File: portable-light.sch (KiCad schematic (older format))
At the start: 11 parts, among them J3 Charger, U1 L78L05_SOT89

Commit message: Schematic's overall structure is finished
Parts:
- added D?: 1N5819, Diode_THT:D_DO-41_SOD81_P12.70mm_Horizontal, symbol portable-light-rescue:1N5819-Diode
- added J?: LOAD, Connector_PinHeader_2.54mm:PinHeader_1x02_P2.54mm_Vertical, symbol portable-light-rescue:LED-Device
- renumbered BT1 to BT?, C27 to C?, C21 to C?, C17 to C?, D9 to D?, D8 to D?, J3 to J?, NT1 to NT?, NT2 to NT?, R26 to R?, U1 to U?
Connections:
- net +8V: now also D?.1 (K)
- net GNDPWR: now also J?.1 (K)
- net at C?.1, D?.2 (A), U?.1 (OUT): now also D?.2 (A)
- new net Buck converter/vout: J?.2 (A)
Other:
- moved on the sheet: BT?, C?, D?, J?, NT?, R?, U?

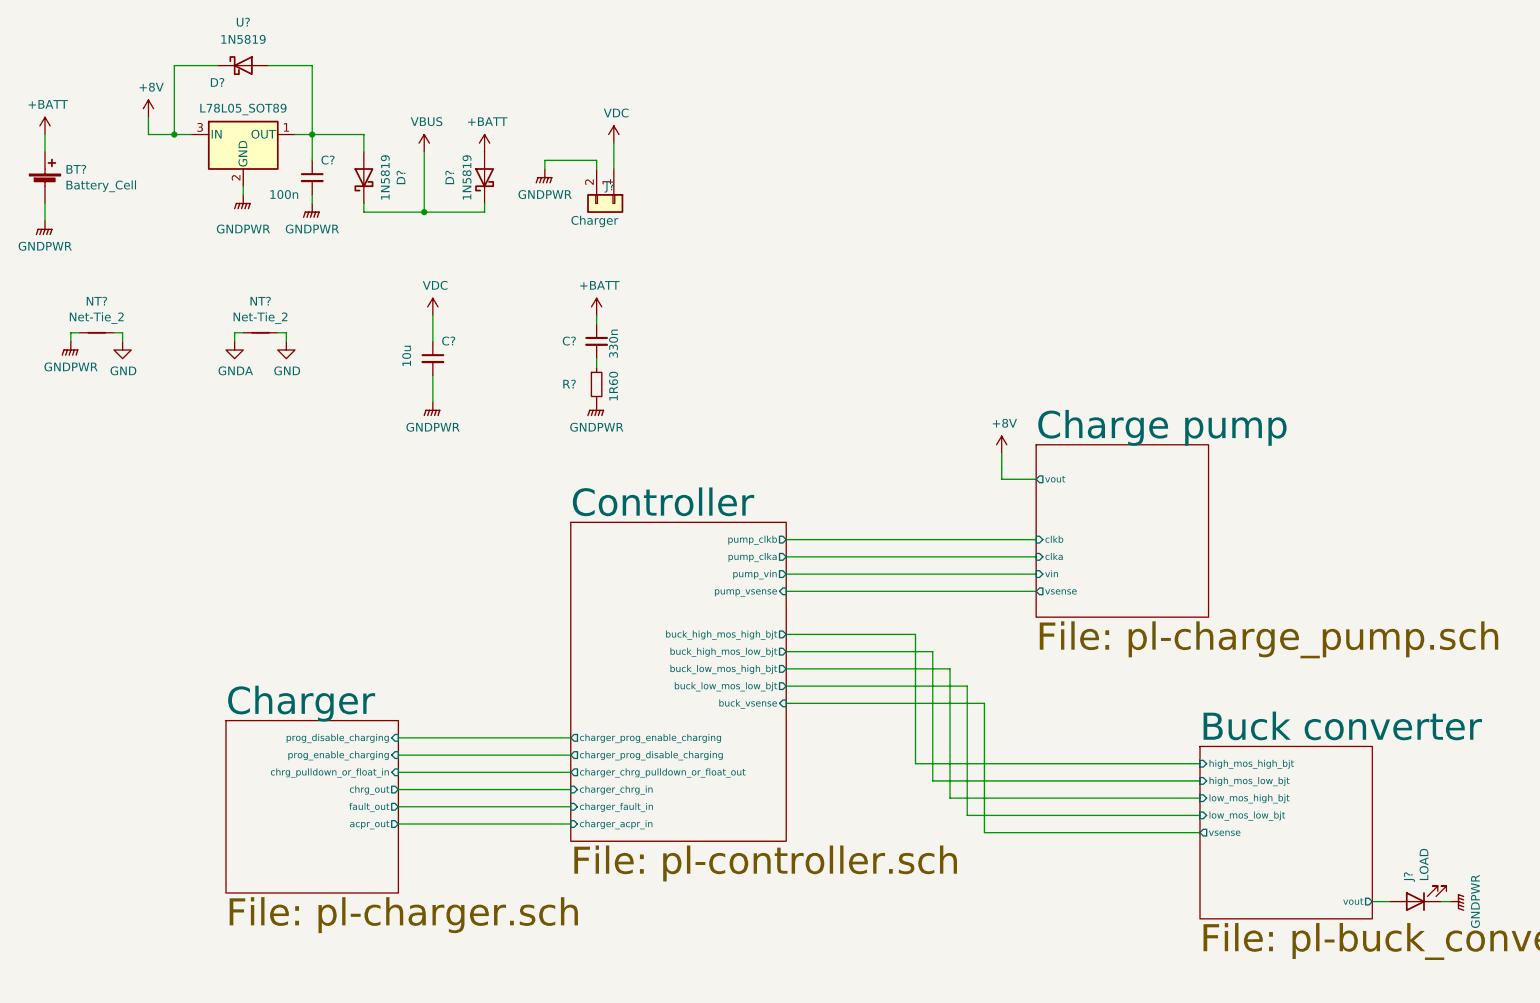
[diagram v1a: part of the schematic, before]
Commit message: Added component values
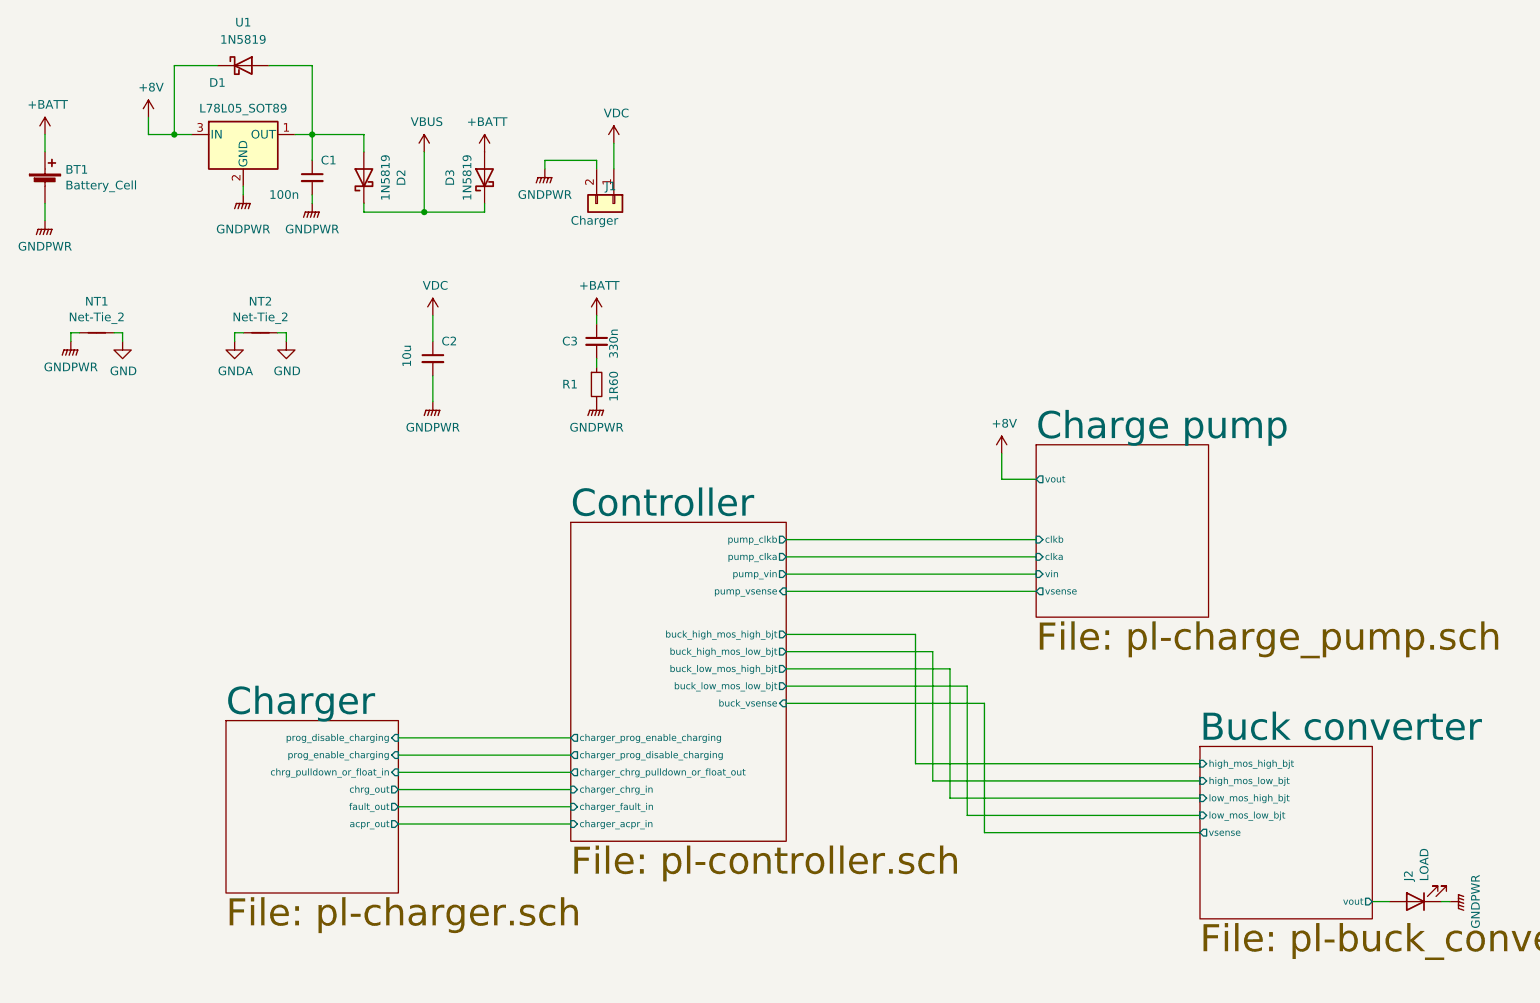
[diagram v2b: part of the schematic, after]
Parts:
- gave numbers to parts that had none: 13

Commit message: Schematics redesigned and fixed
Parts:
- removed C2: 10u, Capacitor_THT:C_Radial_D5.0mm_H7.0mm_P2.00mm, symbol portable-light-rescue:C_Small-Device
- removed C3: 330n, Capacitor_SMD:C_1206_3216Metric_Pad1.42x1.75mm_HandSolder, symbol portable-light-rescue:C_Small-Device
- removed D1, D2, D3: 1N5819, Diode_THT:D_DO-41_SOD81_P12.70mm_Horizontal, symbol portable-light-rescue:1N5819-Diode
- removed J1: Charger, Connector_PinHeader_2.54mm:PinHeader_1x02_P2.54mm_Vertical, symbol portable-light-rescue:Conn_01x02-Connector_Generic
- removed NT1, NT2: Net-Tie_2, NetTie:NetTie-2_SMD_Pad0.5mm, symbol portable-light-rescue:Net-Tie_2-Device
- removed U1: L78L05_SOT89, Package_TO_SOT_SMD:SOT-89-3, symbol portable-light-rescue:L78L05_SOT89-Regulator_Linear
- added J2: conn_sense_pump_2, Ribbon_Cable:Ribbon_2, symbol Connector_Generic:Conn_01x02
- added J3: conn_sense_buck_2, Ribbon_Cable:Ribbon_2, symbol Connector_Generic:Conn_01x02
- added J4: conn_batt_2, Connector_PinHeader_2.54mm:PinHeader_1x02_P2.54mm_Vertical, symbol Connector_Generic:Conn_01x02
- added J5: conn_batt_1, Connector_PinHeader_2.54mm:PinHeader_1x02_P2.54mm_Vertical, symbol Connector_Generic:Conn_01x02
- added J6: conn_sense_pump_1, Ribbon_Cable:Ribbon_2, symbol Connector_Generic:Conn_01x02
- added J7: conn_sense_buck_1, Ribbon_Cable:Ribbon_2, symbol Connector_Generic:Conn_01x02
- added J8: interboard-interface_2, Ribbon_Cable:Ribbon_8, symbol Connector_Generic:Conn_01x08
- added J9: interboard-interface_1, Ribbon_Cable:Ribbon_8, symbol Connector_Generic:Conn_01x08
- added NT1: Net-Tie_4_Cross, NetTie:NetTie-4_SMD_Pad0.5mm, symbol Device:Net-Tie_4_Cross
- C1: value 100n -> 330n
- renumbered J2 to J1
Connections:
- net labels added: +BATT-1, +BATT-2, +PUMP-1, +PUMP-2, GND-CHARGER, GNDPWR-2, buck_high_mos_high_bjt_1, buck_high_mos_high_bjt_2, buck_high_mos_low_bjt_1, buck_high_mos_low_bjt_2, buck_low_mos_high_bjt_1, buck_low_mos_high_bjt_2, buck_low_mos_low_bjt_1, buck_low_mos_low_bjt_2, gnd_vsense_buck_1, gnd_vsense_pump_1, pump_clka_1, pump_clka_2, pump_clkb_1, pump_clkb_2, pump_onoff_1, pump_onoff_2, vsense_buck_1, vsense_buck_2, vsense_pump_1, vsense_pump_2
- net labels removed: +8V, +BATT, VBUS, VDC
- wire segments 65 -> 41
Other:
- moved on the sheet: J1

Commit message: Cleaned up the PCB a little bit, Fixed some errors in schematics
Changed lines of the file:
@@
 Text Label 10100 2200 0    39   ~ 0
 buck_high_mos_high_bjt_2
+Text Label 10100 1900 0    39   ~ 0
+pump_clka_2
 Text Label 10100 1800 0    39   ~ 0
-pump_clka_2
-Text Label 10100 1900 0    39   ~ 0
 pump_clkb_2
 Text Label 10100 2000 0    39   ~ 0
 pump_onoff_2
+Text Label 10100 2400 0    39   ~ 0
+buck_low_mos_low_bjt_2
 Text Label 10100 2500 0    39   ~ 0
-buck_low_mos_low_bjt_2
-Text Label 10100 2400 0    39   ~ 0
 buck_low_mos_high_bjt_2
 Text Label 10100 2300 0    39   ~ 0

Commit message: Seperated the two PCBs successfully, All DRC errors fixed, gotta double check the circuit
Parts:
- removed NT1: Net-Tie_4_Cross, NetTie:NetTie-4_SMD_Pad0.5mm, symbol Device:Net-Tie_4_Cross
- added NT1: Net-Tie_3_Tee, NetTie:NetTie-3_SMD_Pad0.5mm, symbol Device:Net-Tie_3_Tee
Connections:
- net labels removed: GNDPWR-2
- wire segments 41 -> 39
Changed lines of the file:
@@
 P 4300 6700
 AR Path="/5F37658B/60438762" Ref="#PWR?"  Part="1"
-AR Path="/60438762" Ref="#PWR05"  Part="1"
-F 0 "#PWR05" H 4300 6500 50  0001 C CNN
+AR Path="/60438762" Ref="#PWR03"  Part="1"
+F 0 "#PWR03" H 4300 6500 50  0001 C CNN
 F 1 "GNDPWR" H 4300 6550 50  0000 C CNN
 F 2 "" H 4300 6650 50  0001 C CNN
@@
 gnd_vsense_buck_1
 $Comp
-L power:GNDA #PWR06
+L power:GNDA #PWR04
 U 1 1 5F835CEE
 P 8250 1800
-F 0 "#PWR06" H 8250 1550 50  0001 C CNN
+F 0 "#PWR04" H 8250 1550 50  0001 C CNN
 F 1 "GNDA" H 8255 1627 50  0000 C CNN
 F 2 "" H 8250 1800 50  0001 C CNN
@@
 $EndComp
 $Comp
-L power:GNDA #PWR07
+L power:GNDA #PWR05
 U 1 1 5F836352
 P 8250 2550
-F 0 "#PWR07" H 8250 2300 50  0001 C CNN
+F 0 "#PWR05" H 8250 2300 50  0001 C CNN
 F 1 "GNDA" H 8255 2377 50  0000 C CNN
 F 2 "" H 8250 2550 50  0001 C CNN
@@
 Text GLabel 10100 5650 2    39   UnSpc ~ 0
 +PUMP-1
-Wire Wire Line
-	2500 4000 2500 3950
 $Comp
 L portable-light-rescue:Battery_Cell-Device BT1
@@
 Text GLabel 2500 3500 1    39   UnSpc ~ 0
 +BATT-2
-$Comp
-L power:PWR_FLAG #FLG?
-U 1 1 5F8D18F2
-P 2500 3950
-AR Path="/5F378869/5F8D18F2" Ref="#FLG?"  Part="1"
-AR Path="/5F8D18F2" Ref="#FLG02"  Part="1"
-F 0 "#FLG02" H 2500 4025 50  0001 C CNN
-F 1 "PWR_FLAG" V 2500 4077 50  0000 L CNN
-F 2 "" H 2500 3950 50  0001 C CNN
-F 3 "~" H 2500 3950 50  0001 C CNN
-	1    2500 3950
-	0    -1   -1   0
-$EndComp
-Connection ~ 2500 3950
-Wire Wire Line
-	2500 3950 2500 3900
-$Comp
-L power:GND #PWR01
-U 1 1 5F8D1DCF
-P 2500 4000
-F 0 "#PWR01" H 2500 3750 50  0001 C CNN
-F 1 "GND" H 2505 3827 50  0000 C CNN
-F 2 "" H 2500 4000 50  0001 C CNN
-F 3 "" H 2500 4000 50  0001 C CNN
-	1    2500 4000
-	1    0    0    -1
-$EndComp
 Wire Wire Line
 	2500 3550 2500 3600
@@
 P 10700 2000
 AR Path="/5F378869/5F8E5DC5" Ref="#FLG?"  Part="1"
-AR Path="/5F8E5DC5" Ref="#FLG05"  Part="1"
-F 0 "#FLG05" H 10700 2075 50  0001 C CNN
+AR Path="/5F8E5DC5" Ref="#FLG06"  Part="1"
+F 0 "#FLG06" H 10700 2075 50  0001 C CNN
 F 1 "PWR_FLAG" V 10700 2300 50  0000 C CNN
 F 2 "" H 10700 2000 50  0001 C CNN
@@
 	10600 2100 10700 2100
 $Comp
-L power:GND #PWR04
-U 1 1 5F90484F
-P 3450 4000
-F 0 "#PWR04" H 3450 3750 50  0001 C CNN
-F 1 "GND" H 3455 3827 50  0000 C CNN
-F 2 "" H 3450 4000 50  0001 C CNN
-F 3 "" H 3450 4000 50  0001 C CNN
-	1    3450 4000
-	1    0    0    -1
-$EndComp
-Text GLabel 2700 4750 0    39   UnSpc ~ 0
-GNDPWR-2
-$Comp
 L power:GNDA #PWR02
 U 1 1 5F922DAB
-P 2950 4450
-F 0 "#PWR02" H 2950 4200 50  0001 C CNN
-F 1 "GNDA" H 2955 4277 50  0000 C CNN
-F 2 "" H 2950 4450 50  0001 C CNN
-F 3 "" H 2950 4450 50  0001 C CNN
-	1    2950 4450
-	-1   0    0    1
-$EndComp
-$Comp
-L power:GND #PWR03
+P 3350 4750
+F 0 "#PWR02" H 3350 4500 50  0001 C CNN
+F 1 "GNDA" H 3355 4577 50  0000 C CNN
+F 2 "" H 3350 4750 50  0001 C CNN
+F 3 "" H 3350 4750 50  0001 C CNN
+	1    3350 4750
+	0    -1   -1   0
+$EndComp
+$Comp
+L power:GND #PWR01
 U 1 1 5F924424
 P 2950 5000
-F 0 "#PWR03" H 2950 4750 50  0001 C CNN
+F 0 "#PWR01" H 2950 4750 50  0001 C CNN
 F 1 "GND" H 2955 4827 50  0000 C CNN
 F 2 "" H 2950 5000 50  0001 C CNN
@@
 	1    0    0    -1
 $EndComp
-Text GLabel 3200 4750 2    39   UnSpc ~ 0
+Text GLabel 2850 4750 0    39   UnSpc ~ 0
 GND-CHARGER
-$Comp
-L Device:Net-Tie_4_Cross NT1
-U 1 1 5F925FDD
-P 2950 4750
-F 0 "NT1" H 2750 4800 50  0000 L CNN
-F 1 "Net-Tie_4_Cross" H 2650 4600 50  0000 L CNN
-F 2 "NetTie:NetTie-4_SMD_Pad0.5mm" H 2950 4750 50  0001 C CNN
-F 3 "~" H 2950 4750 50  0001 C CNN
-	1    2950 4750
-	1    0    0    -1
-$EndComp
-Wire Wire Line
-	2950 4850 2950 5000
-Wire Wire Line
-	2700 4750 2850 4750
-Wire Wire Line
-	3050 4750 3200 4750
+Wire Wire Line
+	2950 4850 2950 4950
+Wire Wire Line
+	3350 4750 3300 4750
 $Comp
 L power:PWR_FLAG #FLG?
 U 1 1 5F93B483
-P 2950 4550
+P 3300 4750
 AR Path="/5F378869/5F93B483" Ref="#FLG?"  Part="1"
-AR Path="/5F93B483" Ref="#FLG03"  Part="1"
-F 0 "#FLG03" H 2950 4625 50  0001 C CNN
-F 1 "PWR_FLAG" V 2950 4677 50  0000 L CNN
-F 2 "" H 2950 4550 50  0001 C CNN
-F 3 "~" H 2950 4550 50  0001 C CNN
-	1    2950 4550
-	0    -1   -1   0
-$EndComp
-Wire Wire Line
-	2950 4450 2950 4550
-Wire Wire Line
-	2950 4550 2950 4650
-Connection ~ 2950 4550
+AR Path="/5F93B483" Ref="#FLG04"  Part="1"
+F 0 "#FLG04" H 3300 4825 50  0001 C CNN
+F 1 "PWR_FLAG" V 3300 4877 50  0000 L CNN
+F 2 "" H 3300 4750 50  0001 C CNN
+F 3 "~" H 3300 4750 50  0001 C CNN
+	1    3300 4750
+	-1   0    0    1
+$EndComp
 $Comp
 L Connector_Generic:Conn_01x02 J4
@@
 	0    -1   -1   0
 $EndComp
-Text GLabel 8250 3250 3    39   UnSpc ~ 0
-GNDPWR-2
 Text GLabel 8500 3350 2    39   UnSpc ~ 0
 +BATT-2
@@
 $EndSheet
 $Comp
-L power:GNDPWR #PWR08
+L power:GNDPWR #PWR06
 U 1 1 5F9A3E93
 P 8250 4450
-F 0 "#PWR08" H 8250 4250 50  0001 C CNN
+F 0 "#PWR06" H 8250 4250 50  0001 C CNN
 F 1 "GNDPWR" H 8254 4296 50  0000 C CNN
 F 2 "" H 8250 4400 50  0001 C CNN
@@
 	8250 4350 8250 4400
 $Comp
-L power:PWR_FLAG #FLG04
+L power:PWR_FLAG #FLG05
 U 1 1 5F9A588E
 P 8250 4400
-F 0 "#FLG04" H 8250 4475 50  0001 C CNN
+F 0 "#FLG05" H 8250 4475 50  0001 C CNN
 F 1 "PWR_FLAG" V 8250 4527 50  0000 L CNN
 F 2 "" H 8250 4400 50  0001 C CNN
@@
 Wire Wire Line
 	8250 4450 8250 4400
+Connection ~ 3300 4750
+Text GLabel 8250 3250 3    39   UnSpc ~ 0
+GND-CHARGER
+Text GLabel 3450 4000 3    39   UnSpc ~ 0
+GND-CHARGER
+Text GLabel 2500 4000 3    39   UnSpc ~ 0
+GND-CHARGER
+$Comp
+L Device:Net-Tie_3_Tee NT1
+U 1 1 5F7846BA
+P 2950 4750
+F 0 "NT1" H 2950 4800 50  0000 C CNN
+F 1 "Net-Tie_3_Tee" H 2950 4900 50  0000 C CNN
+F 2 "NetTie:NetTie-3_SMD_Pad0.5mm" H 2950 4750 50  0001 C CNN
+F 3 "~" H 2950 4750 50  0001 C CNN
+	1    2950 4750
+	1    0    0    -1
+$EndComp
+Wire Wire Line
+	3050 4750 3300 4750
+$Comp
+L power:PWR_FLAG #FLG?
+U 1 1 5F7A1FD2
+P 2950 4950
+AR Path="/5F378869/5F7A1FD2" Ref="#FLG?"  Part="1"
+AR Path="/5F7A1FD2" Ref="#FLG03"  Part="1"
+F 0 "#FLG03" H 2950 5025 50  0001 C CNN
+F 1 "PWR_FLAG" V 2950 5077 50  0000 L CNN
+F 2 "" H 2950 4950 50  0001 C CNN
+F 3 "~" H 2950 4950 50  0001 C CNN
+	1    2950 4950
+	0    -1   -1   0
+$EndComp
+Connection ~ 2950 4950
+Wire Wire Line
+	2950 4950 2950 5000
+Wire Wire Line
+	2500 3900 2500 4000
 $EndSCHEMATC
